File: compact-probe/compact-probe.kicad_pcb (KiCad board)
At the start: 2 copper layers, 47.5 x 47.5 mm, 9 parts, among them J1 Conn_02x05_Counter_Clockwise, J2 SM04B-SRSS-TB(LF)(SN), J3 SM04B-SRSS-TB(LF)(SN), U1 TruStability_SPI, U2 TruStability_SPI, U3 TruStability_SPI, U4 ESP32-S3-WROOM-1-N16R2, U5 PQFN50P200X200X80-10N, X1 baro_cap

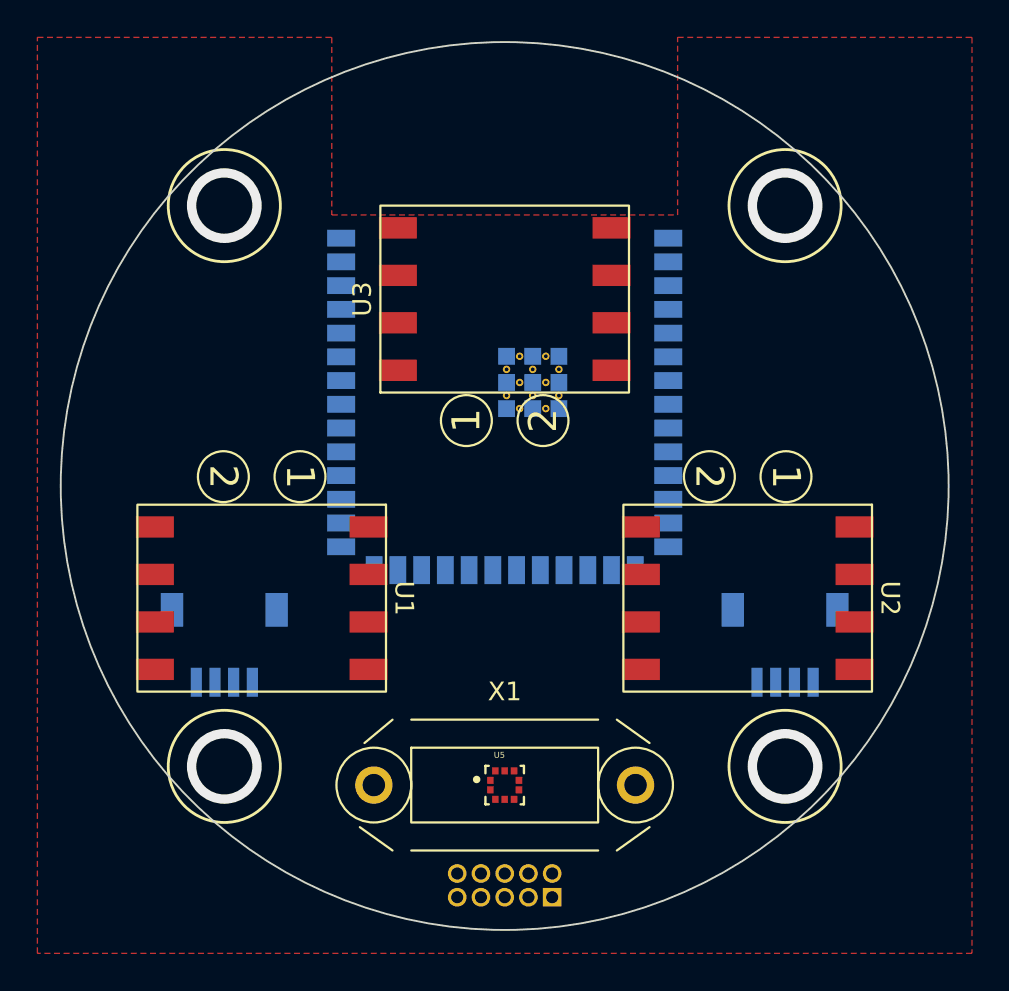
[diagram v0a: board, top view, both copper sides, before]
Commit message: Completed a first pass of the routing.
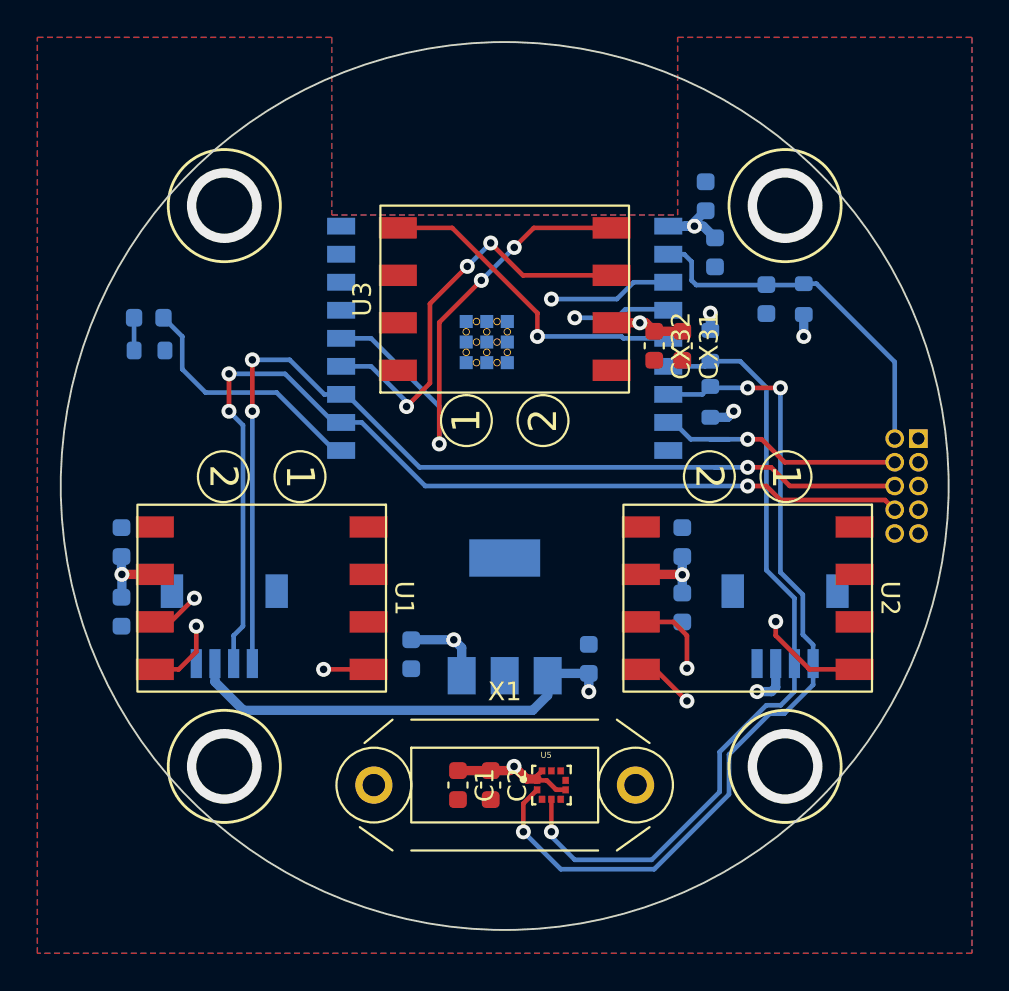
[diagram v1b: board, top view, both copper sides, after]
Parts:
- added C1: 4.7uF, Capacitor_SMD:C_0603_1608Metric, F.Cu at (-2.50, 16.0)
- added C2: 0.1uF, Capacitor_SMD:C_0603_1608Metric, F.Cu at (-0.75, 16.0)
- added C3: 10uF, Capacitor_SMD:C_0603_1608Metric, B.Cu at (4.50, 9.25)
- added C4: 1uF, Capacitor_SMD:C_0603_1608Metric, B.Cu at (14.0, -10.0)
- added C5: 10uF, Capacitor_SMD:C_0603_1608Metric, B.Cu at (-5.00, 9.00)
- added C6: 10uF, Capacitor_SMD:C_0603_1608Metric, B.Cu at (11.2, -12.5)
- added C7: 0.1uF, Capacitor_SMD:C_0603_1608Metric, B.Cu at (10.8, -15.5)
- added CX11: 4.7uF, Capacitor_SMD:C_0603_1608Metric, B.Cu at (-20.5, 6.72)
- added CX12: 0.1uF, Capacitor_SMD:C_0603_1608Metric, B.Cu at (-20.5, 3.00)
- added CX21: 4.7uF, Capacitor_SMD:C_0603_1608Metric, B.Cu at (9.50, 6.50)
- added CX22: 0.1uF, Capacitor_SMD:C_0603_1608Metric, B.Cu at (9.50, 3.00)
- added CX31: 4.7uF, Capacitor_SMD:C_0603_1608Metric, F.Cu at (9.50, -7.50)
- added CX32: 4.7uF, Capacitor_SMD:C_0603_1608Metric, F.Cu at (8.00, -7.50)
- added D1: LED, LED_SMD:LED_0603_1608Metric, B.Cu at (-19.0, -9.00)
- added R1: 10k, Resistor_SMD:R_0603_1608Metric, B.Cu at (16.0, -10.0)
- added R2: 750, Resistor_SMD:R_0603_1608Metric, B.Cu at (-19.0, -7.25)
- added R3: 4.7k, Resistor_SMD:R_0603_1608Metric, B.Cu at (11.0, -7.50)
- added R4: 4.7k, Resistor_SMD:R_0603_1608Metric, B.Cu at (11.0, -4.50)
- added U6: LT1963AxST-3.3, Package_TO_SOT_SMD:SOT-223-3_TabPin2, B.Cu at (0.00, 7.00)
- U4: value ESP32-S3-WROOM-1-N16R2 -> ESP32-C3-WROOM-02-H4; footprint compact-probe:XCVR_ESP32-S3-WROOM-1-N16R2 -> compact-probe:MODULE_ESP32-C3-WROOM-02-H4
- U5: value PQFN50P200X200X80-10N -> BMP388
- moved J1 30.3 mm to (21.5, 0.00), turned to 180 degrees
- moved J2 30.0 mm to (-15.0, 9.50)
- moved J3 30.0 mm to (15.0, 9.50)
- moved U4 3.00 mm to (0.00, -11.0)
- moved U5 2.50 mm to (2.50, 16.0)
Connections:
- J1 pad 1: +5V -> GND
- J1 pad 10: unconnected-(J1-Pad10) -> MCU_EN
- J1 pad 5: GND -> +5V
- J1 pad 7: unconnected-(J1-Pad7) -> RXD
- J1 pad 8: unconnected-(J1-Pad8) -> TXD
- J1 pad 9: unconnected-(J1-Pad9) -> MCU_IO9
- J2 pad 3: unconnected-(J2-Pad3) -> RXD
- J2 pad 4: unconnected-(J2-Pad4) -> TXD
- J2 pad S1: Net-(J2-PadS1) -> GND
- J2 pad S2: Net-(J2-PadS1) -> GND
- J3 pad 3: unconnected-(J3-Pad3) -> SDA
- J3 pad 4: unconnected-(J3-Pad4) -> SCL
- J3 pad S1: Net-(J3-PadS1) -> GND
- J3 pad S2: Net-(J3-PadS1) -> GND
- U1 pad 3: unconnected-(U1-Pad3) -> MISO
- U1 pad 4: unconnected-(U1-Pad4) -> SCLK
- U1 pad 5: unconnected-(U1-Pad5) -> SS1
- U2 pad 3: unconnected-(U2-Pad3) -> MISO
- U2 pad 4: unconnected-(U2-Pad4) -> SCLK
- U2 pad 5: unconnected-(U2-Pad5) -> SS2
- U3 pad 3: unconnected-(U3-Pad3) -> MISO
- U3 pad 4: unconnected-(U3-Pad4) -> SCLK
- U3 pad 5: unconnected-(U3-Pad5) -> SS3
- U4 pad 1: Net-(U4-Pad1) -> +3V3
- U4 pad 10: unconnected-(U4-Pad10) -> Net-(D1-Pad2)
- U4 pad 11: unconnected-(U4-Pad11) -> RXD
- U4 pad 12: unconnected-(U4-Pad12) -> TXD
- U4 pad 13: unconnected-(U4-Pad13) -> MISO
- U4 pad 14: unconnected-(U4-Pad14) -> SCLK
- U4 pad 19: unconnected-(U4-Pad19) -> GND
- U4 pad 2: unconnected-(U4-Pad2) -> MCU_EN
- U4 pad 20: unconnected-(U4-Pad20) -> GND
- U4 pad 21: unconnected-(U4-Pad21) -> GND
- U4 pad 22: unconnected-(U4-Pad22) -> GND
- U4 pad 23: unconnected-(U4-Pad23) -> GND
- U4 pad 24: unconnected-(U4-Pad24) -> GND
- U4 pad 25: unconnected-(U4-Pad25) -> GND
- U4 pad 26: unconnected-(U4-Pad26) -> GND
- U4 pad 27: unconnected-(U4-Pad27) -> GND
- U4 pad 28: unconnected-(U4-Pad28) -> GND
- U4 pad 29: unconnected-(U4-Pad29) -> GND
- U4 pad 3: unconnected-(U4-Pad3) -> SS1
- U4 pad 30: unconnected-(U4-Pad30) -> GND
- U4 pad 31: unconnected-(U4-Pad31) -> GND
- U4 pad 32: unconnected-(U4-Pad32) -> GND
- U4 pad 33: unconnected-(U4-Pad33) -> GND
- U4 pad 34: unconnected-(U4-Pad34) -> GND
- U4 pad 35: unconnected-(U4-Pad35) -> GND
- U4 pad 36: unconnected-(U4-Pad36) -> GND
- U4 pad 37: unconnected-(U4-Pad37) -> GND
- U4 pad 38: unconnected-(U4-Pad38) -> GND
- U4 pad 39: unconnected-(U4-Pad39) -> GND
- U4 pad 4: unconnected-(U4-Pad4) -> SS2
- U4 pad 5: unconnected-(U4-Pad5) -> SS3
- U4 pad 6: unconnected-(U4-Pad6) -> SDA
- U4 pad 7: unconnected-(U4-Pad7) -> SCL
- U4 pad 8: unconnected-(U4-Pad8) -> MCU_IO9
- U4 pad 9: unconnected-(U4-Pad9) -> GND
- U5 pad 1: unconnected-(U5-Pad1) -> +3V3
- U5 pad 10: unconnected-(U5-Pad10) -> +3V3
- U5 pad 2: unconnected-(U5-Pad2) -> SCL
- U5 pad 3: Net-(U5-Pad3) -> GND
- U5 pad 4: unconnected-(U5-Pad4) -> SDA
- U5 pad 5: unconnected-(U5-Pad5) -> GND
- U5 pad 6: unconnected-(U5-Pad6) -> +3V3
- U5 pad 8: Net-(U5-Pad3) -> GND
- U5 pad 9: Net-(U5-Pad3) -> GND
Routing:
- net SCLK: track 0.00 -> 70.7 mm, vias 0 -> 5
- net MISO: track 0.00 -> 67.5 mm, vias 0 -> 5
- net RXD: track 0.00 -> 54.6 mm, vias 0 -> 3
- net TXD: track 0.00 -> 53.7 mm, vias 0 -> 3
- net SS1: track 0.00 -> 47.4 mm, vias 0 -> 2
- net SCL: track 0.00 -> 47.0 mm, vias 0 -> 3
- net SDA: track 0.00 -> 43.3 mm, vias 0 -> 1
- net +3V3: track 0.00 -> 33.5 mm, vias 0 -> 10
- net SS2: track 0.00 -> 31.6 mm, vias 0 -> 2
- net +5V: track 0.00 -> 24.0 mm, vias 0 -> 1
- net MCU_EN: track 0.00 -> 19.2 mm
- net SS3: track 0.00 -> 17.6 mm, vias 0 -> 1
- net MCU_IO9: track 0.00 -> 14.0 mm, vias 0 -> 1
- net Net-(D1-Pad2): track 0.00 -> 13.5 mm
- net Net-(D1-Pad1): track 0.00 -> 1.75 mm
- added copper zone on In1.Cu, net +3V3
- added copper zone on In2.Cu, net +5V
- added copper zone on B.Cu, net GND
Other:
- copper layers 2 -> 4

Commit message: More routing and silk screen improvements.
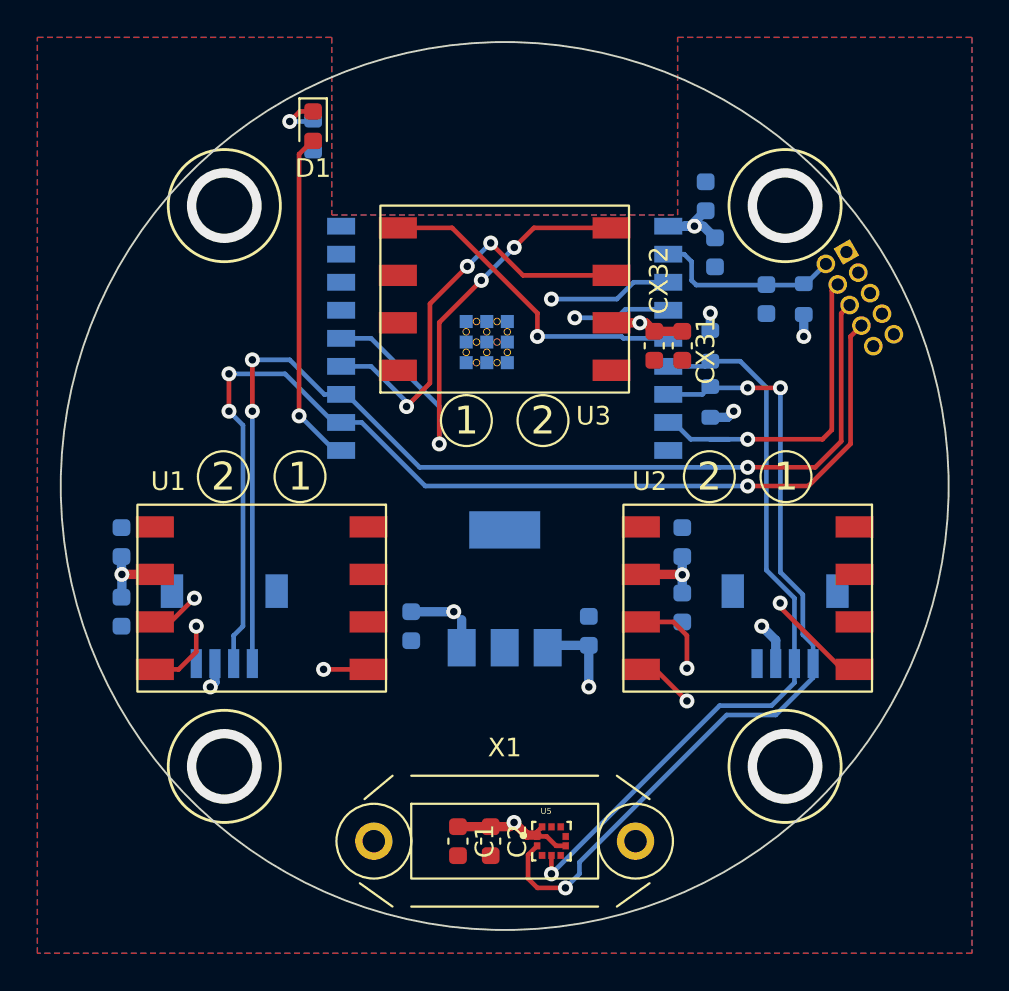
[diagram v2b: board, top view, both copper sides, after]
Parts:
- D1: moved to F.Cu
- moved R2 14.5 mm to (-10.2, -18.8), turned to -90 degrees
- moved D1 13.5 mm to (-10.2, -19.2), turned to -90 degrees
- moved J1 10.3 mm to (19.0, -10.0), turned to -150 degrees
- moved C1 3.00 mm to (-2.50, 19.0)
- moved C2 3.00 mm to (-0.75, 19.0)
- moved U5 3.00 mm to (2.50, 19.0)
- moved X1 3.00 mm to (0.00, 19.0)
- moved C3 1.50 mm to (4.50, 7.75)
- moved C5 1.50 mm to (-5.00, 7.50)
- moved U6 1.50 mm to (0.00, 5.50)
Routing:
- net +5V: track 24.0 -> 5.83 mm, vias 1 -> 2
- net MISO: track 67.5 -> 80.4 mm
- net SCLK: track 70.7 -> 82.8 mm
- net MCU_EN: track 19.2 -> 10.2 mm
- net TXD: track 53.7 -> 58.4 mm
- net RXD: track 54.6 -> 59.3 mm
- net Net-(D1-Pad2): track 13.5 -> 18.1 mm, vias 0 -> 1
- net MCU_IO9: track 14.0 -> 18.2 mm
- net SDA: track 43.3 -> 40.6 mm
- net SCL: track 47.0 -> 44.9 mm
- net Net-(D1-Pad1): track 1.75 -> 2.75 mm, vias 0 -> 1

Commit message: Updated routing and board layout.
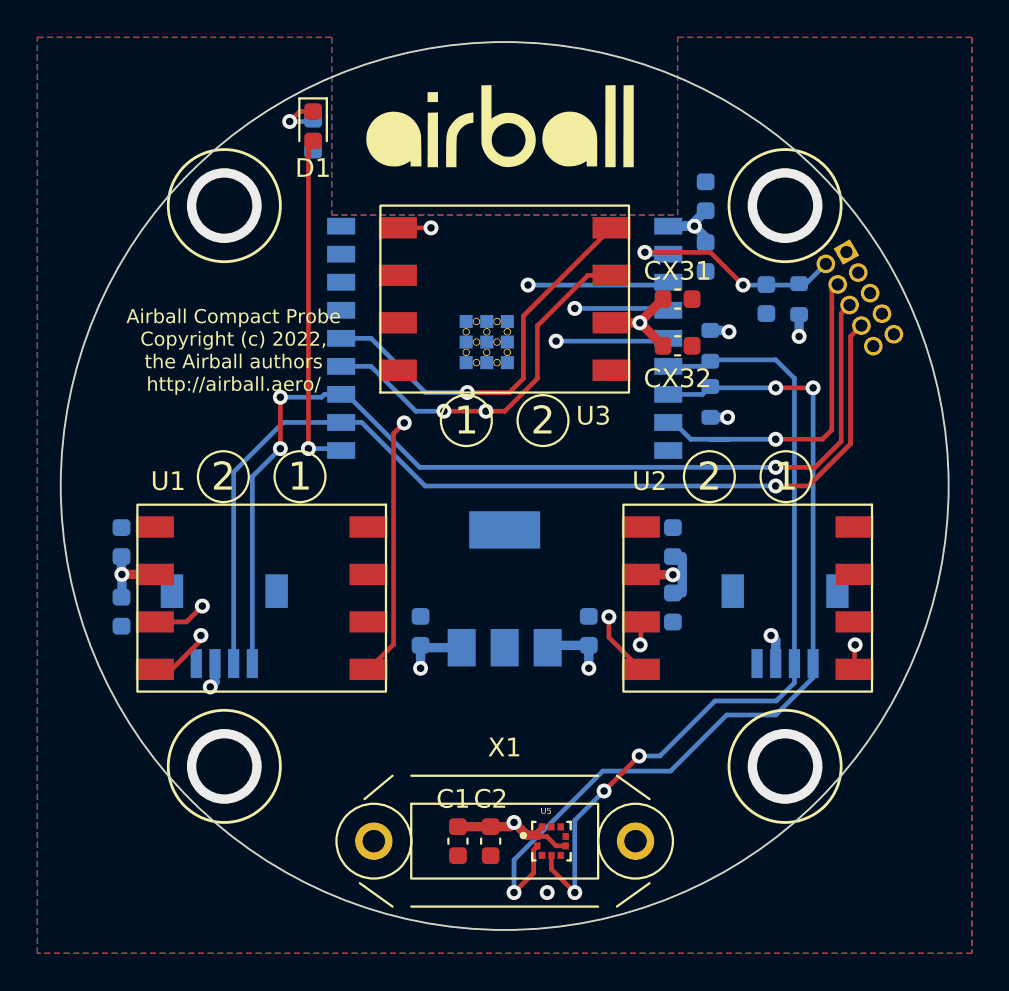
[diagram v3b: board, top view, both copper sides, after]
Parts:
- added G***: LOGO, compact-probe:airball_logo, F.Cu at (-0.15, -18.5)
- added G***: LOGO, compact-probe:qwiic_logo, B.Cu at (15.0, 3.25)
- moved CX31 2.51 mm to (9.25, -10.0), turned to 0 degrees
- moved CX32 1.25 mm to (9.25, -7.50), turned to 0 degrees
- moved C5 0.56 mm to (-4.50, 7.75), turned to 90 degrees
- moved C6 0.56 mm to (10.8, -12.2)
- moved CX21 0.50 mm to (9.00, 6.50)
- moved CX22 0.50 mm to (9.00, 3.00)
- moved R1 0.25 mm to (15.8, -10.0)
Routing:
- net MISO: track 80.4 -> 58.5 mm, vias 5 -> 4
- net SCLK: track 82.8 -> 64.1 mm, vias 5 -> 3
- net SS1: track 47.4 -> 33.7 mm
- net RXD: track 59.3 -> 53.7 mm, vias 3 -> 1
- net SDA: track 40.6 -> 44.7 mm, vias 1 -> 3
- net TXD: track 58.4 -> 54.9 mm
- net SCL: track 44.9 -> 48.3 mm
- net MCU_EN: track 10.2 -> 12.2 mm, vias 0 -> 2
- net SS3: track 17.6 -> 19.5 mm, vias 1 -> 2
- net +3V3: track 33.5 -> 32.5 mm
- net +5V: track 5.83 -> 4.83 mm
- net SS2: track 31.3 -> 30.6 mm
- net GND: vias 4 -> 5
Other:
- board text added: "Airball Compact Probe Copyright (c) 2022, the Airball authors http://airball.aero/"

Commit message: More work on the silk screen.
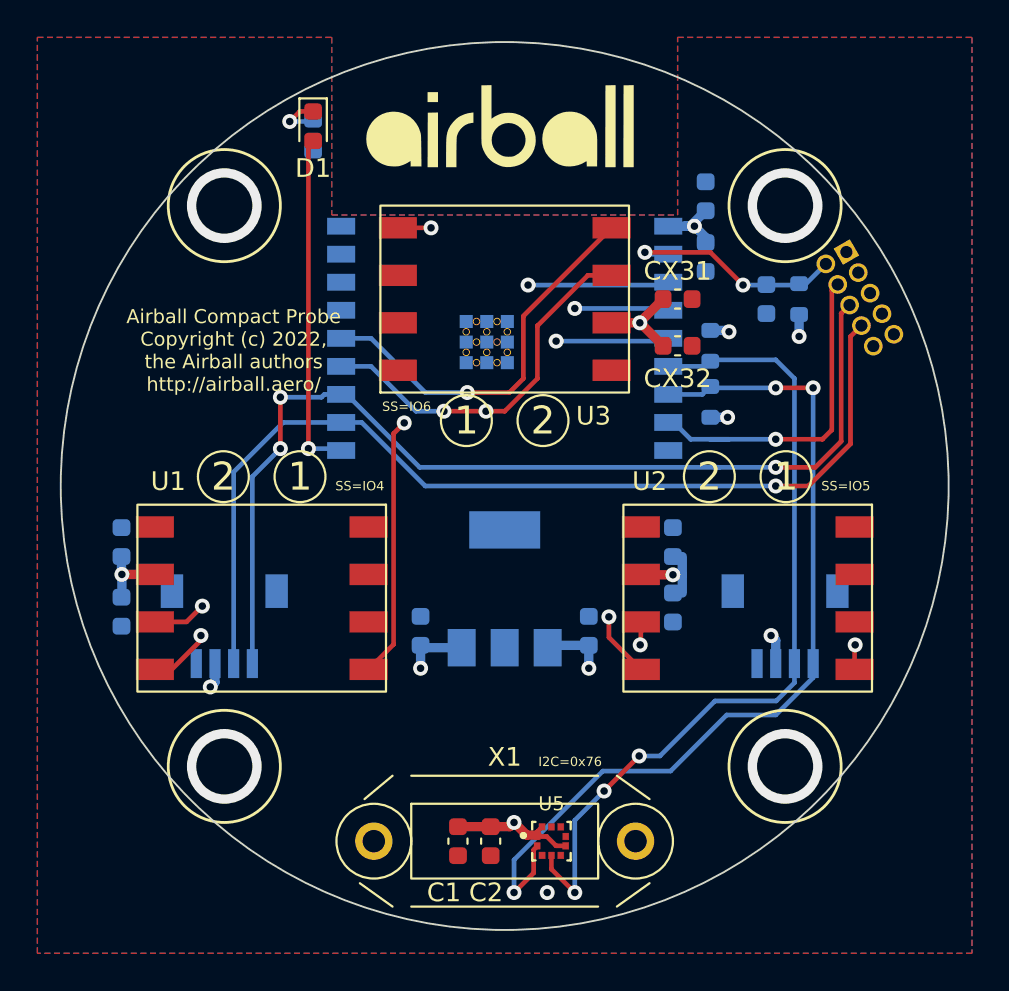
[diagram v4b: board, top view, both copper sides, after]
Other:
- board text added: "I2C=0x76"
- board text added: "SS=IO4"
- board text added: "SS=IO5"
- board text added: "SS=IO6"
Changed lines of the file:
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@@
     (property "Sheetname" "")
     (attr smd)
-    (fp_text reference "C1" (at -2.25 0.25) (layer "F.SilkS")
+    (fp_text reference "C1" (at 2.75 0.75) (layer "F.SilkS")
       (effects (font (size 1 1) (thickness 0.15)))
     )
@@
     (clearance 0.05)
     (attr through_hole)
-    (fp_text reference "U5" (at -0.284383 -1.605376) (layer "F.SilkS")
-      (effects (font (size 0.320434 0.320434) (thickness 0.15)))
+    (fp_text reference "U5" (at 0 -2) (layer "F.SilkS")
+      (effects (font (size 0.75 0.75) (thickness 0.15)))
     )
     (fp_text value "BMP388" (at 3.07187 1.499081) (layer "F.Fab")
@@
     (property "Sheetname" "")
     (attr through_hole)
-    (fp_text reference "X1" (at 0 -5 unlocked) (layer "F.SilkS")
+    (fp_text reference "X1" (at 0 -4.5 unlocked) (layer "F.SilkS")
       (effects (font (size 1 1) (thickness 0.15)))
     )
@@
     (property "Sheetname" "")
     (attr smd)
-    (fp_text reference "C2" (at -2.25 0 180) (layer "F.SilkS")
+    (fp_text reference "C2" (at 2.75 0.25 180) (layer "F.SilkS")
       (effects (font (size 1 1) (thickness 0.15)))
     )
@@
   (gr_line (start 0 -25) (end 0 30) (layer "Dwgs.User") (width 0.15))
   (gr_circle (center 0 0) (end 23.75 0) (layer "Edge.Cuts") (width 0.1) (fill none))
+  (gr_text "SS=IO5" (at 18.25 0) (layer "F.SilkS")
+    (effects (font (size 0.5 0.5) (thickness 0.05)))
+  )
+  (gr_text "SS=IO6" (at -5.25 -4.25) (layer "F.SilkS")
+    (effects (font (size 0.5 0.5) (thickness 0.05)))
+  )
+  (gr_text "I2C=0x76" (at 3.5 14.75) (layer "F.SilkS")
+    (effects (font (size 0.5 0.5) (thickness 0.05)))
+  )
   (gr_text "Airball Compact Probe\nCopyright (c) 2022,\nthe Airball authors\nhttp://airball.aero/" (at -14.5 -7.25) (layer "F.SilkS")
     (effects (font (size 0.75 0.75) (thickness 0.15)))
   )
+  (gr_text "SS=IO4" (at -7.75 0) (layer "F.SilkS")
+    (effects (font (size 0.5 0.5) (thickness 0.05)))
+  )
   (via (at 15 -15) (size 4) (drill 3) (layers "F.Cu" "B.Cu") (free) (net 1))
